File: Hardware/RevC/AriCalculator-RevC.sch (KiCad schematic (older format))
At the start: 0 parts

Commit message: work in progress
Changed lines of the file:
@@
 Sheet 1 6
 Title "AriCalulator"
-Date "3 nov 2014"
+Date "4 nov 2014"
 Rev "RevC"
 Comp "Dirk Heisswolf"
@@
 NoConn ~ -23300 -9850
 $Sheet
-S 1300 2700 1600 1000
+S 1300 2700 1600 1200
 U 544A6FCE
 F0 "Supply" 50
@@
 $EndSheet
 $Sheet
-S 5400 2400 1600 1300
+S 5400 2400 1550 1500
 U 544A66C8
 F0 "Keypad" 50
 F1 "AriCalculator-RevC-Keypad.sch" 50
-F2 "KEYPAD_ROW_F" O L 5400 3100 60
-F3 "KEYPAD_ROW_E" O L 5400 3200 60
-F4 "KEYPAD_ROW_D" O L 5400 3300 60
-F5 "KEYPAD_ROW_C" O L 5400 3400 60
-F6 "KEYPAD_ROW_B" O L 5400 3500 60
-F7 "KEYPAD_ROW_A" O L 5400 3600 60
-F8 "KEYPAD_COL_0" T L 5400 2900 60
-F9 "KEYPAD_COL_1" T L 5400 2800 60
-F10 "KEYPAD_COL_2" T L 5400 2700 60
-F11 "KEYPAD_COL_3" T L 5400 2600 60
-F12 "KEYPAD_COL_4" B L 5400 2500 60
+F2 "KEYPAD_ROW_F" O L 5400 3300 60
+F3 "KEYPAD_ROW_E" O L 5400 3400 60
+F4 "KEYPAD_ROW_D" O L 5400 3500 60
+F5 "KEYPAD_ROW_C" O L 5400 3600 60
+F6 "KEYPAD_ROW_B" O L 5400 3700 60
+F7 "KEYPAD_ROW_A" O L 5400 3800 60
+F8 "KEYPAD_COL_0" T L 5400 3000 60
+F9 "KEYPAD_COL_1" T L 5400 2900 60
+F10 "KEYPAD_COL_2" T L 5400 2800 60
+F11 "KEYPAD_COL_3" T L 5400 2700 60
+F12 "KEYPAD_COL_4" B L 5400 2600 60
+F13 "KEYPAD_ROW_G" O L 5400 3200 60
+F14 "KEYPAD_COL_5" B L 5400 2500 60
 $EndSheet
 $Sheet
@@
 F5 "UART_TXD" I R 2900 1750 60
 $EndSheet
-$Sheet
-S 3350 1400 1600 2300
-U 544A64C5
-F0 "MCU" 50
-F1 "AriCalculator-RevC-MCU.sch" 50
-F2 "KEYPAD_COL_0" T R 4950 2900 60
-F3 "KEYPAD_COL_1" T R 4950 2800 60
-F4 "KEYPAD_COL_2" T R 4950 2700 60
-F5 "KEYPAD_COL_3" T R 4950 2600 60
-F6 "KEYPAD_COL_4" T R 4950 2500 60
-F7 "KEYPAD_ROW_A" I R 4950 3600 60
-F8 "KEYPAD_ROW_B" I R 4950 3500 60
-F9 "KEYPAD_ROW_C" I R 4950 3400 60
-F10 "KEYPAD_ROW_D" I R 4950 3300 60
-F11 "KEYPAD_ROW_E" I R 4950 3200 60
-F12 "KEYPAD_ROW_F" I R 4950 3100 60
-F13 "UART_CTS" O L 3350 1950 60
-F14 "DISPLAY_BACKLIGHT" O R 4950 2000 60
-F15 "UART_RTS" I L 3350 2050 60
-F16 "UART_TXD" O L 3350 1750 60
-F17 "UART_RXD" I L 3350 1850 60
-F18 "DISPLAY_SS" O R 4950 1700 60
-F19 "DISPLAY_SCK" O R 4950 1600 60
-F20 "DISPLAY_MOSI" O R 4950 1500 60
-F21 "DISPLAY_A0" O R 4950 1800 60
-F22 "DISPLAY_RESET" O R 4950 1900 60
-$EndSheet
 Wire Wire Line
 	4950 2500 5400 2500
@@
 Wire Wire Line
 	4950 2900 5400 2900
-Wire Wire Line
-	4950 3100 5400 3100
-Wire Wire Line
-	4950 3200 5400 3200
 Wire Wire Line
 	4950 3300 5400 3300
@@
 Wire Wire Line
 	2900 2050 3350 2050
+$Sheet
+S 3350 1400 1600 2500
+U 544A64C5
+F0 "MCU" 50
+F1 "AriCalculator-RevC-MCU.sch" 50
+F2 "KEYPAD_COL_0" T R 4950 3000 60
+F3 "KEYPAD_COL_1" T R 4950 2900 60
+F4 "KEYPAD_COL_2" T R 4950 2800 60
+F5 "KEYPAD_COL_3" T R 4950 2700 60
+F6 "KEYPAD_COL_4" T R 4950 2600 60
+F7 "KEYPAD_ROW_A" I R 4950 3800 60
+F8 "KEYPAD_ROW_B" I R 4950 3700 60
+F9 "KEYPAD_ROW_C" I R 4950 3600 60
+F10 "KEYPAD_ROW_D" I R 4950 3500 60
+F11 "KEYPAD_ROW_E" I R 4950 3400 60
+F12 "KEYPAD_ROW_F" I R 4950 3300 60
+F13 "UART_CTS" O L 3350 1950 60
+F14 "DISPLAY_BACKLIGHT" O R 4950 2000 60
+F15 "UART_RTS" I L 3350 2050 60
+F16 "UART_TXD" O L 3350 1750 60
+F17 "UART_RXD" I L 3350 1850 60
+F18 "DISPLAY_SS" O R 4950 1700 60
+F19 "DISPLAY_SCK" O R 4950 1600 60
+F20 "DISPLAY_MOSI" O R 4950 1500 60
+F21 "DISPLAY_A0" O R 4950 1800 60
+F22 "DISPLAY_RESET" O R 4950 1900 60
+F23 "KEYPAD_COL_5" B R 4950 2500 60
+F24 "KEYPAD_ROW_G" I R 4950 3200 60
+$EndSheet
+Wire Wire Line
+	4950 3800 5400 3800
+Wire Wire Line
+	4950 3700 5400 3700
+Wire Wire Line
+	4950 3000 5400 3000
+Wire Wire Line
+	4950 3200 5400 3200
 $EndSCHEMATC

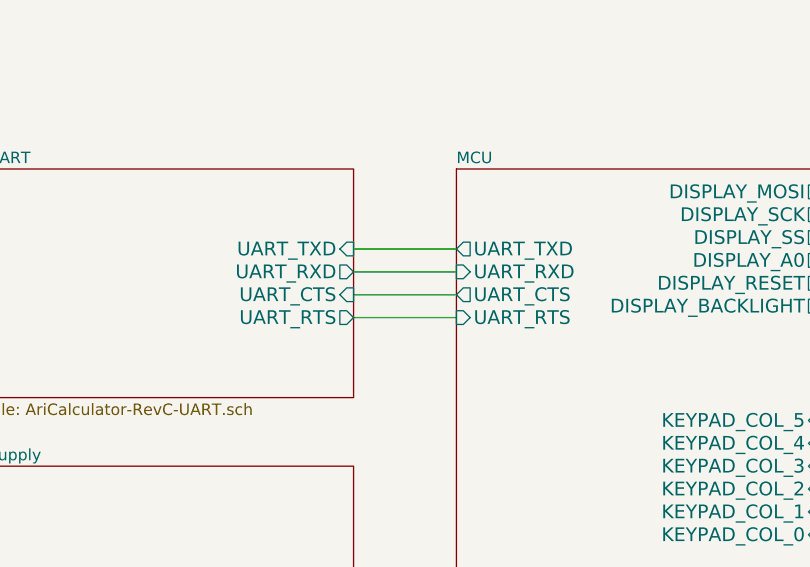
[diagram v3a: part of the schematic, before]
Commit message: started RevC layout
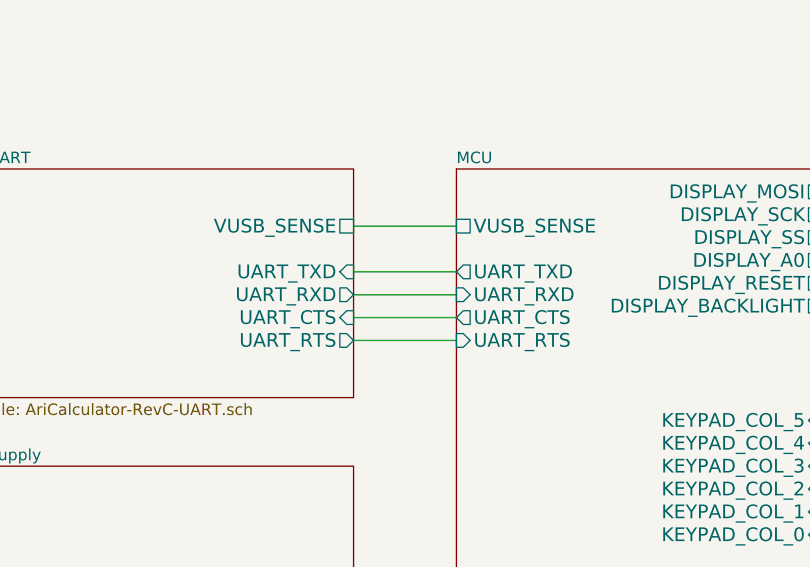
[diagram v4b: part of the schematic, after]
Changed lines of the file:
@@
 F0 "UART" 50
 F1 "AriCalculator-RevC-UART.sch" 50
-F2 "UART_CTS" I R 2900 1950 60
-F3 "UART_RTS" O R 2900 2050 60
-F4 "UART_RXD" O R 2900 1850 60
-F5 "UART_TXD" I R 2900 1750 60
+F2 "UART_CTS" I R 2900 2050 60
+F3 "UART_RTS" O R 2900 2150 60
+F4 "UART_RXD" O R 2900 1950 60
+F5 "UART_TXD" I R 2900 1850 60
+F6 "VUSB_SENSE" U R 2900 1650 60
 $EndSheet
 Wire Wire Line
@@
 	4950 1500 5400 1500
 Wire Wire Line
-	2900 1750 3350 1750
-Wire Wire Line
 	2900 1850 3350 1850
 Wire Wire Line
@@
 F11 "KEYPAD_ROW_E" I R 4950 3400 60
 F12 "KEYPAD_ROW_F" I R 4950 3300 60
-F13 "UART_CTS" O L 3350 1950 60
+F13 "UART_CTS" O L 3350 2050 60
 F14 "DISPLAY_BACKLIGHT" O R 4950 2000 60
-F15 "UART_RTS" I L 3350 2050 60
-F16 "UART_TXD" O L 3350 1750 60
-F17 "UART_RXD" I L 3350 1850 60
+F15 "UART_RTS" I L 3350 2150 60
+F16 "UART_TXD" O L 3350 1850 60
+F17 "UART_RXD" I L 3350 1950 60
 F18 "DISPLAY_SS" O R 4950 1700 60
 F19 "DISPLAY_SCK" O R 4950 1600 60
@@
 F23 "KEYPAD_COL_5" B R 4950 2500 60
 F24 "KEYPAD_ROW_G" I R 4950 3200 60
+F25 "VUSB_SENSE" U L 3350 1650 60
 $EndSheet
 Wire Wire Line
@@
 Wire Wire Line
 	4950 3200 5400 3200
+Wire Wire Line
+	2900 2150 3350 2150
+Wire Wire Line
+	2900 1650 3350 1650
 $EndSCHEMATC
